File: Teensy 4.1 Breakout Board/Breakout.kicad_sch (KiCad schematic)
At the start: 53 parts, among them J1 CAN, J10 RTD_Speaker, J11 Current Sensor Power source, J12 RTD_button, J2 12V Power, J3 APPS1, J4 APPS2, J5 Brake_Pressure_Front, J6 Brake_Pressure_Rear, J7 Nextion, J8 ESP32, J9 Brake_Light, Q1 2N7002, Q3 2N7002, U1 SN65HVD230, U3 Teensy4.1, U4 TPS62163DSG, U5 MPU6050

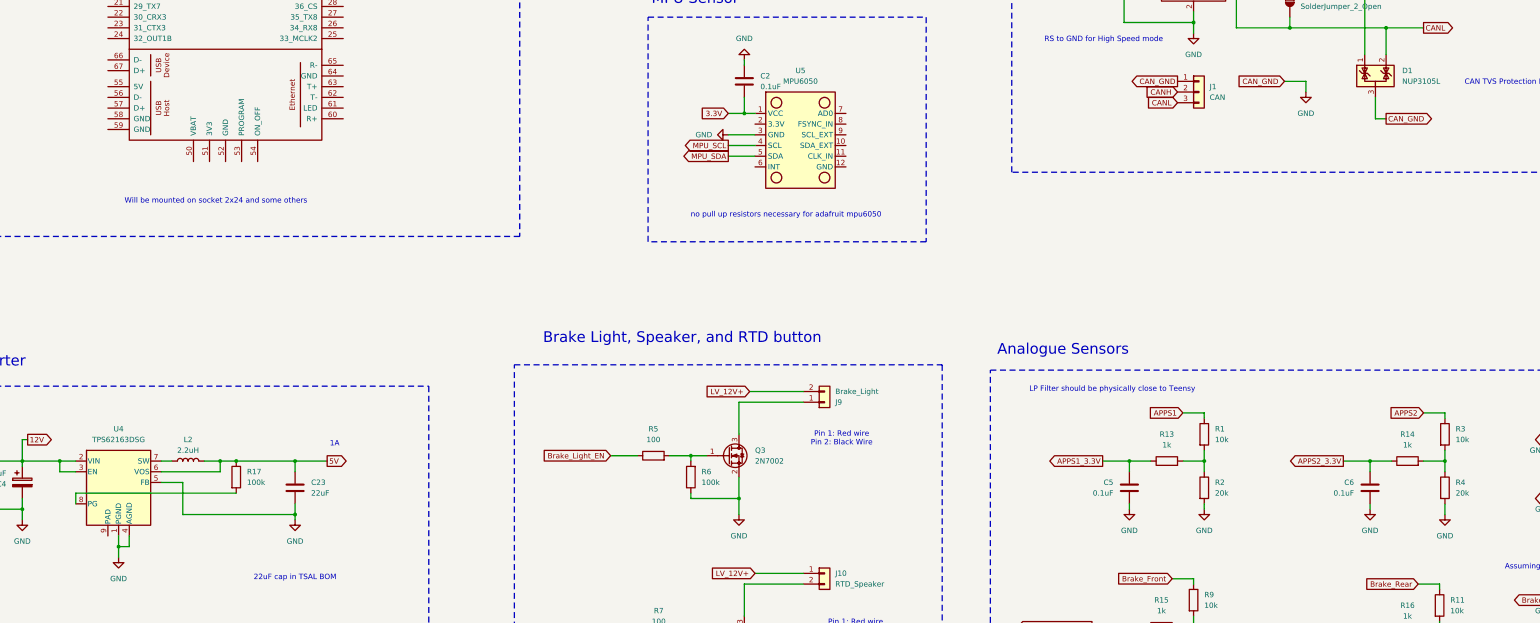
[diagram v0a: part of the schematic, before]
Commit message: Slave with SMD and no other fuses
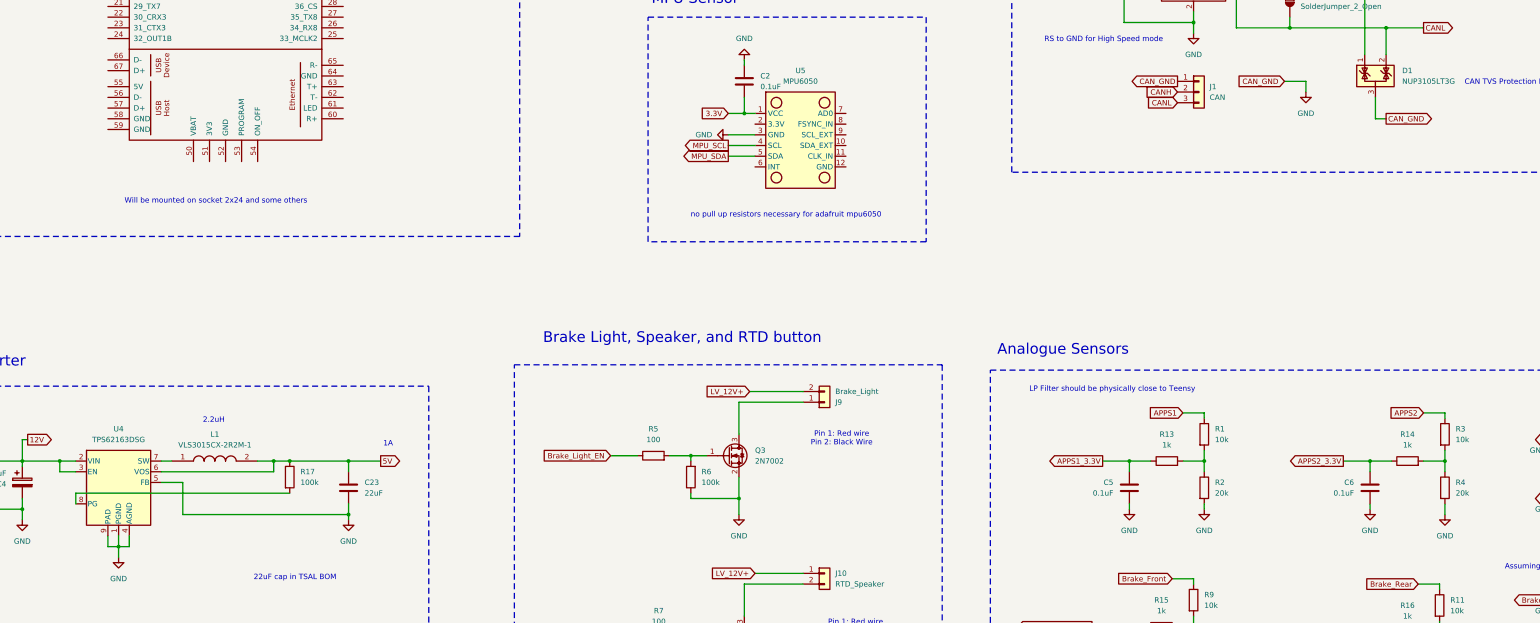
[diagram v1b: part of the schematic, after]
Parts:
- removed L2: 2.2uH, XFL3012222:XFL3012222MEC, symbol Device:L
- added L1: VLS3015CX-2R2M-1, Kicad_Libraries:VLS3015, symbol VLS3015CX-2R2M-1:VLS3015CX-2R2M-1
- D1: value NUP3105L -> NUP3105LT3G
- Q1, Q3: Part Number (none) -> 2N7002
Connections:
- net 5V: now also L1.2
- net GND: now also U4.9 (PAD)
- net at U4.7 (SW): now also L1.1
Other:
- note added: "2.2uH"
- moved on the sheet: C23, R17

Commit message: master and slave updated
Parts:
- C1, C10, C2, C3, C5, C6, C7, C8: Part Number (none) -> FA18X7R1H104KNU00
- D1: Part Number (none) -> NUP3105LT3G
- U1: Part Number (none) -> SN65HVD230
- U3: Part Number (none) -> Teensy4.1
- U4: Part Number (none) -> TPS62163DSG
- U5: Part Number (none) -> MPU6050
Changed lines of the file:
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@@
 			)
 		)
+		(property "Part Number" "FA18X7R1H104KNU00"
+			(at 365.76 297.18 0)
+			(effects
+				(font
+					(size 1.27 1.27)
+				)
+				(hide yes)
+			)
+		)
 		(pin "1"
 		)
@@
 			)
 		)
+		(property "Part Number" "Teensy4.1"
+			(at 151.13 186.69 0)
+			(effects
+				(font
+					(size 1.27 1.27)
+				)
+				(hide yes)
+			)
+		)
 		(pin "5"
 		)
@@
 			)
 		)
+		(property "Part Number" "FA18X7R1H104KNU00"
+			(at 193.04 128.27 0)
+			(effects
+				(font
+					(size 1.27 1.27)
+				)
+				(hide yes)
+			)
+		)
 		(pin "1"
 		)
@@
 			)
 		)
+		(property "Part Number" "FA18X7R1H104KNU00"
+			(at 364.49 336.55 0)
+			(effects
+				(font
+					(size 1.27 1.27)
+				)
+				(hide yes)
+			)
+		)
 		(pin "1"
 		)
@@
 			)
 		)
+		(property "Part Number" "TPS62163DSG"
+			(at 125.73 298.45 0)
+			(effects
+				(font
+					(size 1.27 1.27)
+				)
+				(hide yes)
+			)
+		)
 		(pin "1"
 		)
@@
 			)
 		)
+		(property "Part Number" "MPU6050"
+			(at 287.02 213.36 0)
+			(effects
+				(font
+					(size 1.27 1.27)
+				)
+				(hide yes)
+			)
+		)
 		(pin "8"
 		)
@@
 			)
 		)
+		(property "Part Number" "FA18X7R1H104KNU00"
+			(at 257.81 363.22 0)
+			(effects
+				(font
+					(size 1.27 1.27)
+				)
+				(hide yes)
+			)
+		)
 		(pin "1"
 		)
@@
 			)
 		)
+		(property "Part Number" "FA18X7R1H104KNU00"
+			(at 381 157.48 0)
+			(effects
+				(font
+					(size 1.27 1.27)
+				)
+				(hide yes)
+			)
+		)
 		(pin "1"
 		)
@@
 			)
 		)
+		(property "Part Number" "FA18X7R1H104KNU00"
+			(at 422.91 337.82 0)
+			(effects
+				(font
+					(size 1.27 1.27)
+				)
+				(hide yes)
+			)
+		)
 		(pin "1"
 		)
@@
 			)
 		)
+		(property "Part Number" "NUP3105LT3G"
+			(at 424.18 199.39 0)
+			(effects
+				(font
+					(size 1.27 1.27)
+				)
+				(hide yes)
+			)
+		)
 		(pin "3"
 		)
@@
 			)
 		)
+		(property "Part Number" "FA18X7R1H104KNU00"
+			(at 274.32 200.66 0)
+			(effects
+				(font
+					(size 1.27 1.27)
+				)
+				(hide yes)
+			)
+		)
 		(pin "1"
 		)
@@
 			)
 		)
+		(property "Part Number" "FA18X7R1H104KNU00"
+			(at 422.91 297.18 0)
+			(effects
+				(font
+					(size 1.27 1.27)
+				)
+				(hide yes)
+			)
+		)
 		(pin "1"
 		)
@@
 			(at 381 173.99 0)
 			(effects
+				(font
+					(size 1.27 1.27)
+				)
+				(hide yes)
+			)
+		)
+		(property "Part Number" "SN65HVD230"
+			(at 381 173.99 0)
+			(effects

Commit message: added author
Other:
- company: (none) -> UCD Formula Student
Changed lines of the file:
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@@
 	(generator_version "9.0")
 	(paper "A2")
+	(title_block
+		(company "UCD Formula Student")
+		(comment 1 "Author: Keelan Reilly")
+	)
 	(rectangle
 		(start 90.17 106.68)
